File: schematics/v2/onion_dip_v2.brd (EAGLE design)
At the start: 41 x 50 mm, 35 parts, among them IC2 DS2432P

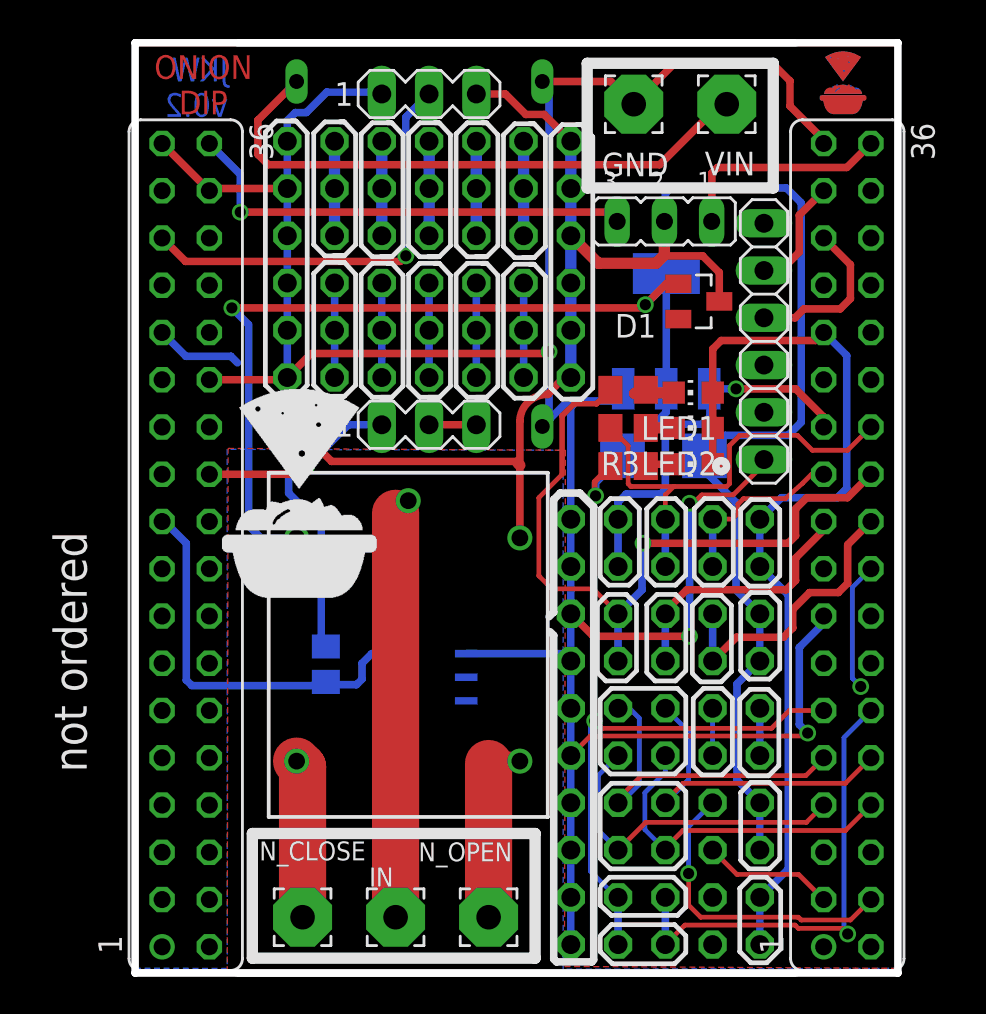
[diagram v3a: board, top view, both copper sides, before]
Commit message: v2, clearance on relay; leds; usb jack; pulldowns
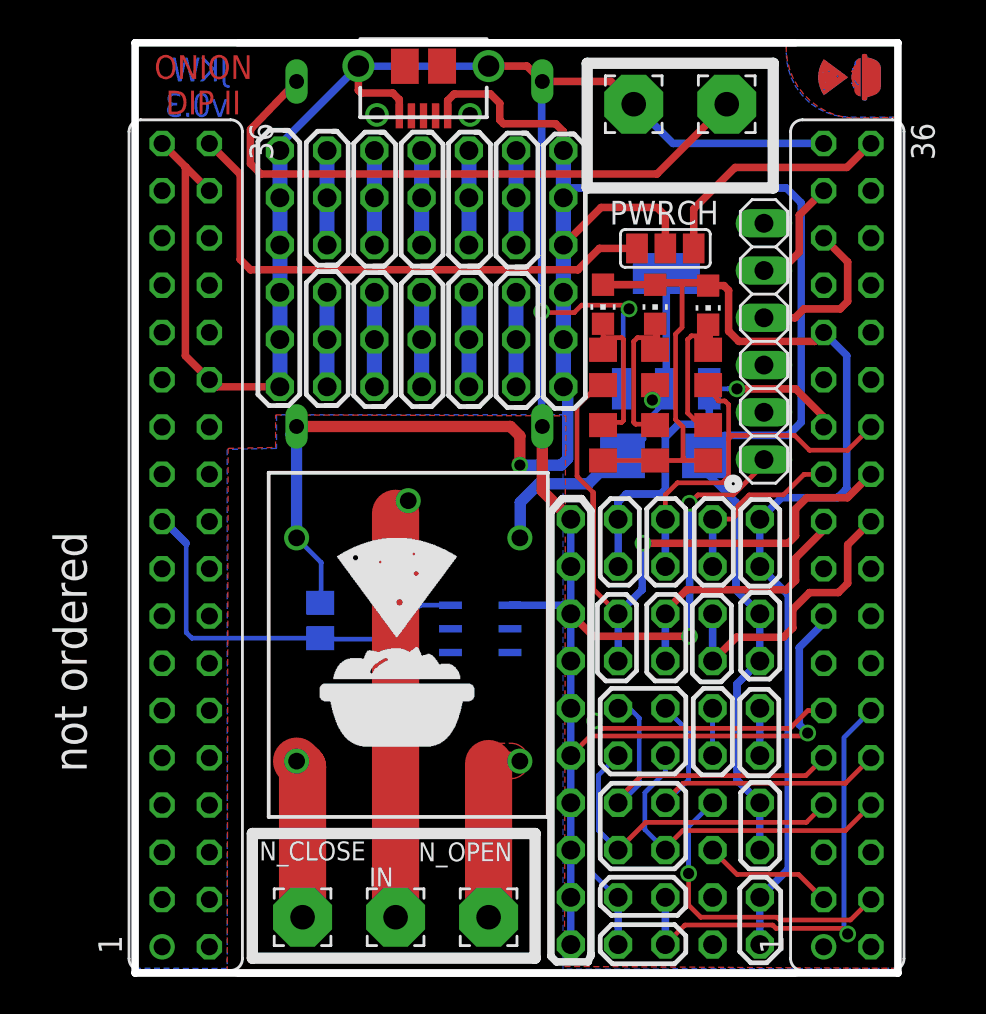
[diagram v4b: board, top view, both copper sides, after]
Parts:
- removed D1: BAS70, diode:SOT23
- removed JP3: (no value), jumper:JP2
- removed SV5, SV8: (no value), con-lstb_no_frame:MA03-1
- added PWRCH: (no value), jumper:SJ_2
- added R4, R5, R6: 10k, rcl:R0805
- added USB: USBUSB-MICROB-SMT-DIP, Spark:USB-MICROB-SMT-DIP
- moved U$5 9.57 mm to (9.90, 12.2)
- moved LED5 8.84 mm to (27.9, 36.0), turned to 180 degrees
- moved LED1 6.79 mm to (25.1, 36.0), turned to 180 degrees
- moved LED2 6.65 mm to (30.8, 35.9), turned to 180 degrees
- moved R7 5.49 mm to (27.9, 32.5), turned to 270 degrees
- moved R3 5.39 mm to (30.8, 32.5), turned to 270 degrees
- moved IC2 3.50 mm to (18.6, 18.5)
- moved R1 2.37 mm to (9.95, 18.9)
- moved R2 1.81 mm to (25.1, 32.5), turned to 270 degrees
- moved SV20 0.64 mm to (15.4, 42.9)
- moved SV21 0.64 mm to (15.4, 37.9)
- moved SV7 0.64 mm to (15.4, 32.8)
- moved U$4 0.46 mm to (38.4, 48.1), turned to 90 degrees
- moved U$6 0.46 mm to (38.4, 48.1), turned to 270 degrees
- renumbered ASDASD to COMM, SV1 to I2C_1, SV4 to SPI2_2, SV9 to SPI2_1
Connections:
- removed net N$2: SV8.2, SV8.3
- net 3V3: no longer SV5.2
- net CHIP_5V: now also PWRCH.1; no longer JP3.1
- net CHR_IN: now also PWRCH.3; no longer JP3.3
- net GND: now also USB.GND, USB.MT1, USB.MT2; no longer SV5.1
- net N$29: now also R6.2
- net N$3: now also R5.2
- net N$4: now also R4.2
- net RELAY_LO: now also U$1.COIL1; no longer D1.1, U$1.COIL0
- net VCC: now also PWRCH.2, U$1.COIL0, USB.VBUS; no longer D1.3, JP3.2, SV5.3, U$1.COIL1
- net Y2: no longer SV8.1
- net _3V3: now also R4.1, R5.1, R6.1
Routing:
- net RELAY_LO: track 57.2 -> 21.0 mm, vias 3 -> 1
- net 3V3: track 23.0 -> 0.00 mm, vias 1 -> 0
- net _3V3: track 50.9 -> 69.0 mm
- net Y2: track 10.4 -> 0.00 mm, vias 1 -> 0
- net N$29: track 1.54 -> 8.58 mm
- net P7: track 7.00 -> 0.00 mm, vias 1 -> 0
- net N$4: track 1.50 -> 7.87 mm
- net GND: track 164.1 -> 169.8 mm, vias 4 -> 5
- net N$3: track 2.73 -> 8.41 mm
- net SDA: track 4.73 -> 0.00 mm
- net CHR_IN: track 24.8 -> 29.0 mm, vias 1 -> 0
- net P1: track 25.2 -> 21.7 mm
- net P3: track 39.0 -> 35.7 mm
- net N$2: track 2.54 -> 0.00 mm
- net VCC: track 119.2 -> 117.0 mm, vias 0 -> 1
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- added copper zone on layer 1, net NOP
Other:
- board text added: "CHIP powered -> 1&2"
- board text added: "Input 5V: Close 3&2"
- board text added: "JKW v0.3"
- board text added: "ONION DIP II"
- board text removed: "JKW v0.2"
- board text removed: "ONION DIP"
